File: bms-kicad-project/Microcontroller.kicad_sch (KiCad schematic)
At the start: 1 part, among them U2 RP2040

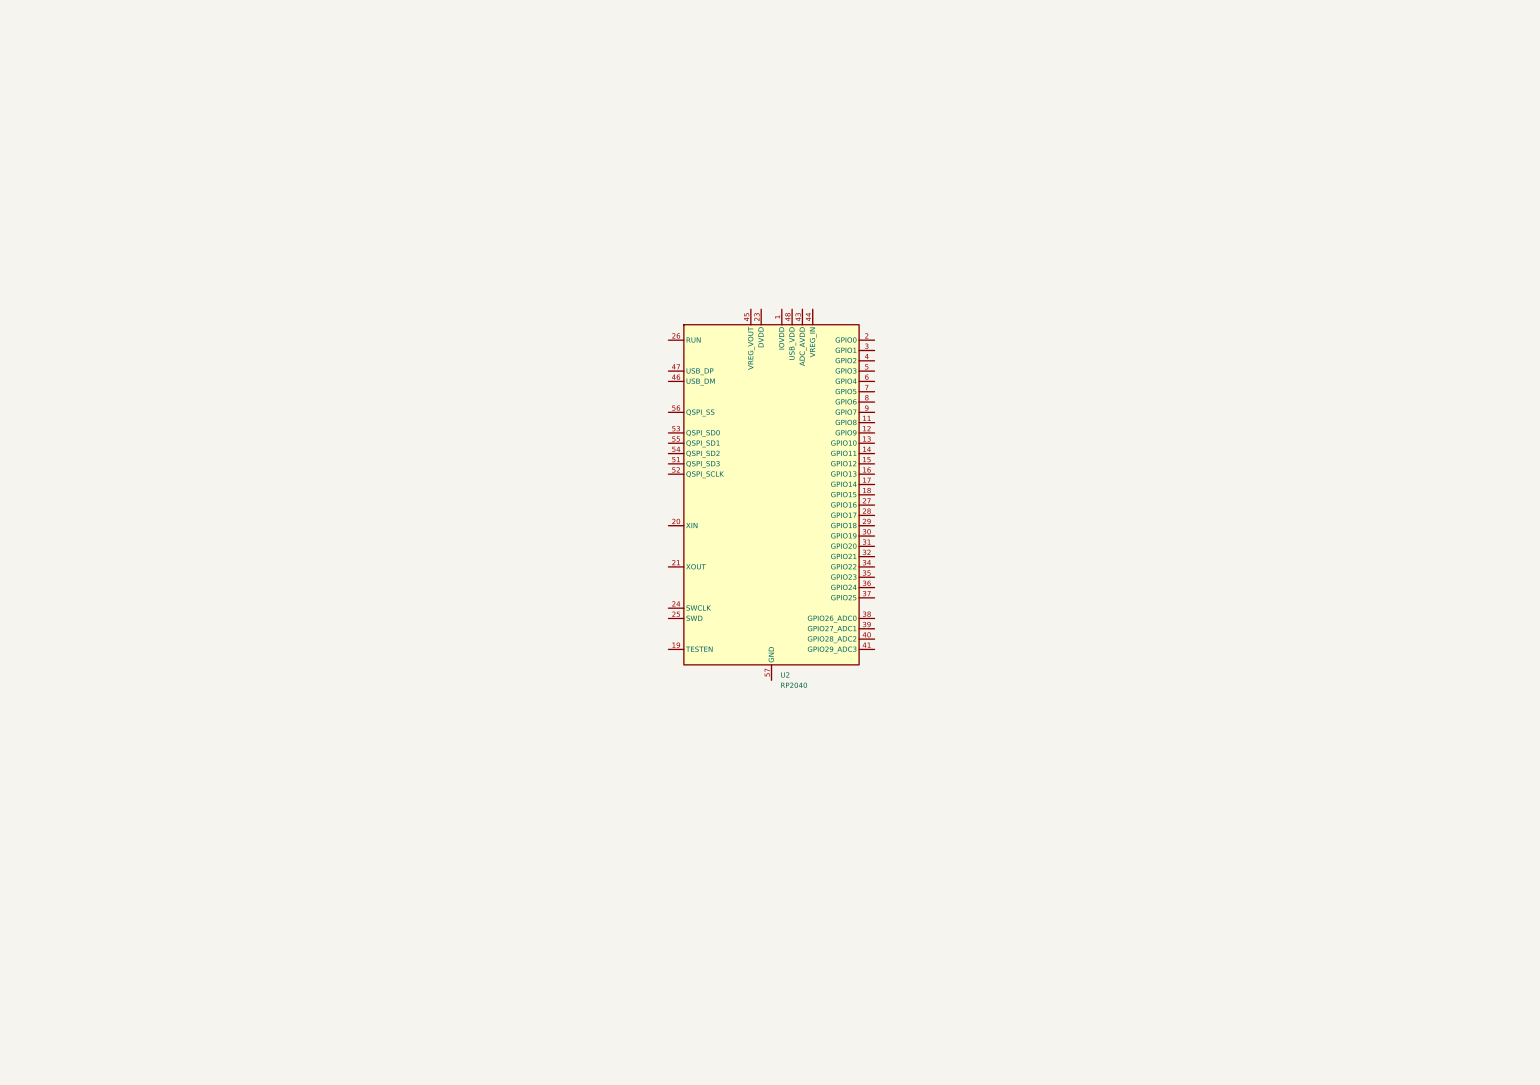
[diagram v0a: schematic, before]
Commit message: feat: added minimal MCU schematic, 3D component model folder
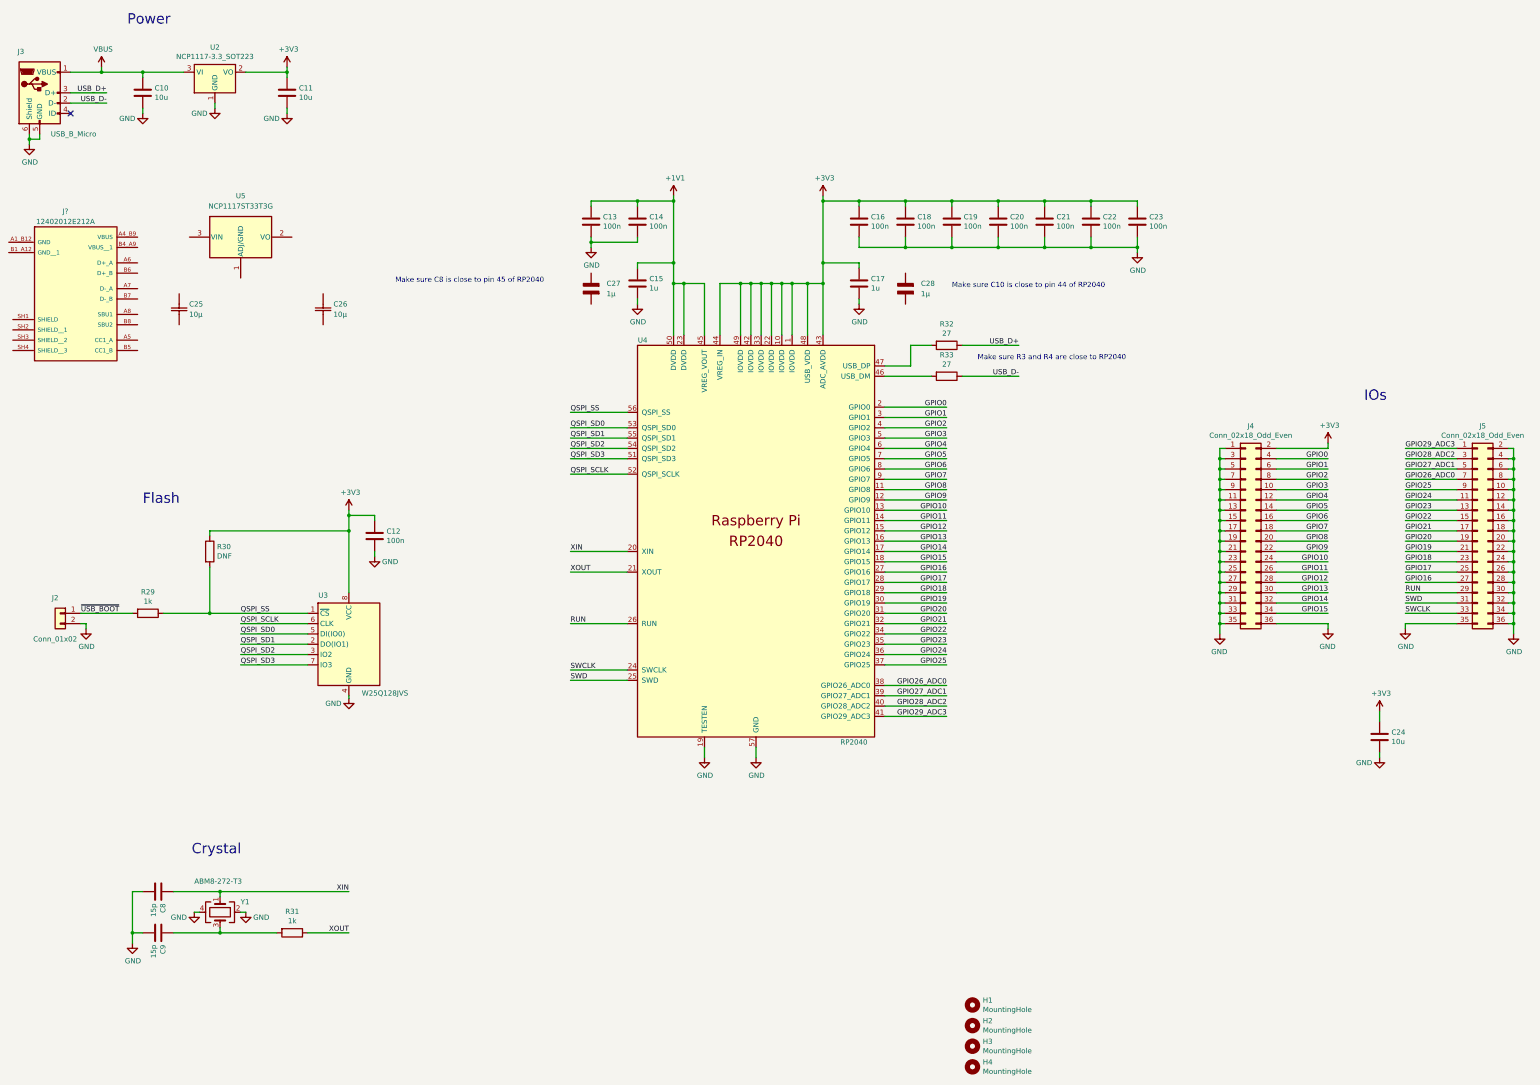
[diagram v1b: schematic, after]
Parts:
- removed U2: RP2040, Package_DFN_QFN:QFN-56-1EP_7x7mm_P0.4mm_EP3.2x3.2mm, symbol MCU_RaspberryPi:RP2040
- added C10, C11, C24: 10u, Capacitor_SMD:C_0805_2012Metric, symbol Device:C
- added C12, C13, C14, C16, C18, C19, C20, C21, C22, C23: 100n, Capacitor_SMD:C_0402_1005Metric, symbol Device:C
- added C15, C17: 1u, Capacitor_SMD:C_0402_1005Metric, symbol Device:C
- added C25, C26: 10µ, FixedWing:CAP_CL21B106KOQNNNE_SAM, symbol FixedWing:CL21B106KOQNNNE
- added C27, C28: 1µ, FixedWing:CAPC2012X140N, symbol FixedWing:GCM21BR71C105KA58L
- added C8, C9: 15p, Capacitor_SMD:C_0402_1005Metric, symbol Device:C
- added H1, H2, H3, H4: MountingHole, MountingHole:MountingHole_2.7mm_M2.5, symbol Mechanical:MountingHole
- added J2: Conn_01x02, Connector_PinHeader_2.54mm:PinHeader_1x02_P2.54mm_Vertical, symbol Connector_Generic:Conn_01x02
- added J3: USB_B_Micro, RP2040_minimal:USB_Micro-B_Amphenol_10103594-0001LF_Horizontal_modified, symbol Connector:USB_B_Micro
- added J4, J5: Conn_02x18_Odd_Even, Connector_PinHeader_2.54mm:PinHeader_2x18_P2.54mm_Vertical, symbol Connector_Generic:Conn_02x18_Odd_Even
- added J?: 12402012E212A, FixedWing:AMPHENOL_12402012E212A, symbol FixedWing:12402012E212A
- added R29, R31: 1k, Resistor_SMD:R_0402_1005Metric, symbol Device:R
- added R30: DNF, Resistor_SMD:R_0402_1005Metric, symbol Device:R
- added R32, R33: 27, Resistor_SMD:R_0402_1005Metric, symbol Device:R
- added U2: NCP1117-3.3_SOT223, Package_TO_SOT_SMD:SOT-223-3_TabPin2, symbol Regulator_Linear:NCP1117-3.3_SOT223
- added U3: W25Q128JVS, Package_SO:SOIC-8_5.23x5.23mm_P1.27mm, symbol Memory_Flash:W25Q128JVS
- added U4: RP2040, FixedWing:RP2040-QFN-56, symbol FixedWing:RP2040
- added U5: NCP1117ST33T3G, FixedWing:SOT223-3_ONS, symbol FixedWing:NCP1117ST33T3G
- added Y1: ABM8-272-T3, Crystal:Crystal_SMD_3225-4Pin_3.2x2.5mm, symbol Device:Crystal_GND24
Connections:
- new net: R33.2, U4.46 (USB_DM)
- new net: R32.2, U4.47 (USB_DP)
- new net: C9.1, R31.2, Y1.3
- new net +1V1: C13.1, C14.1, C15.1, U4.23 (DVDD), U4.45 (VREG_VOUT), U4.50 (DVDD)
- new net +3V3: C11.1, C12.1, C16.1, C17.1, C18.1, C19.1, C20.1, C21.1, C22.1, C23.1, C24.1, J4.2 (Pin_2), R30.1, U2.2 (VO), U3.8 (VCC), U4.1 (IOVDD), U4.10 (IOVDD), U4.22 (IOVDD), U4.33 (IOVDD), U4.42 (IOVDD), U4.43 (ADC_AVDD), U4.44 (VREG_IN), U4.48 (USB_VDD), U4.49 (IOVDD)
- new net GND: C10.2, C11.2, C12.2, C13.2, C14.2, C15.2, C16.2, C17.2, C18.2, C19.2, C20.2, C21.2, C22.2, C23.2, C24.2, C8.2, C9.2, J2.2 (Pin_2), J3.5 (GND), J3.6 (Shield), J4.1 (Pin_1), J4.11 (Pin_11), J4.13 (Pin_13), J4.15 (Pin_15), J4.17 (Pin_17), J4.19 (Pin_19), J4.21 (Pin_21), J4.23 (Pin_23), J4.25 (Pin_25), J4.27 (Pin_27), J4.29 (Pin_29), J4.3 (Pin_3), J4.31 (Pin_31), J4.33 (Pin_33), J4.35 (Pin_35), J4.36 (Pin_36), J4.5 (Pin_5), J4.7 (Pin_7), J4.9 (Pin_9), J5.10 (Pin_10), J5.12 (Pin_12), J5.14 (Pin_14), J5.16 (Pin_16), J5.18 (Pin_18), J5.2 (Pin_2), J5.20 (Pin_20), J5.22 (Pin_22), J5.24 (Pin_24), J5.26 (Pin_26), J5.28 (Pin_28), J5.30 (Pin_30), J5.32 (Pin_32), J5.34 (Pin_34), J5.35 (Pin_35), J5.36 (Pin_36), J5.4 (Pin_4), J5.6 (Pin_6), J5.8 (Pin_8), U2.1 (GND), U3.4 (GND), U4.19 (TESTEN), U4.57 (GND), Y1.2, Y1.4
- new net GPIO0: J4.4 (Pin_4), U4.2 (GPIO0)
- new net GPIO1: J4.6 (Pin_6), U4.3 (GPIO1)
- new net GPIO10: J4.24 (Pin_24), U4.13 (GPIO10)
- new net GPIO11: J4.26 (Pin_26), U4.14 (GPIO11)
- new net GPIO12: J4.28 (Pin_28), U4.15 (GPIO12)
- new net GPIO13: J4.30 (Pin_30), U4.16 (GPIO13)
- new net GPIO14: J4.32 (Pin_32), U4.17 (GPIO14)
- new net GPIO15: J4.34 (Pin_34), U4.18 (GPIO15)
- new net GPIO16: J5.27 (Pin_27), U4.27 (GPIO16)
- new net GPIO17: J5.25 (Pin_25), U4.28 (GPIO17)
- new net GPIO18: J5.23 (Pin_23), U4.29 (GPIO18)
- new net GPIO19: J5.21 (Pin_21), U4.30 (GPIO19)
- new net GPIO2: J4.8 (Pin_8), U4.4 (GPIO2)
- new net GPIO20: J5.19 (Pin_19), U4.31 (GPIO20)
- new net GPIO21: J5.17 (Pin_17), U4.32 (GPIO21)
- new net GPIO22: J5.15 (Pin_15), U4.34 (GPIO22)
- new net GPIO23: J5.13 (Pin_13), U4.35 (GPIO23)
- new net GPIO24: J5.11 (Pin_11), U4.36 (GPIO24)
- new net GPIO25: J5.9 (Pin_9), U4.37 (GPIO25)
- new net GPIO26_ADC0: J5.7 (Pin_7), U4.38 (GPIO26_ADC0)
- new net GPIO27_ADC1: J5.5 (Pin_5), U4.39 (GPIO27_ADC1)
- new net GPIO28_ADC2: J5.3 (Pin_3), U4.40 (GPIO28_ADC2)
- new net GPIO29_ADC3: J5.1 (Pin_1), U4.41 (GPIO29_ADC3)
- new net GPIO3: J4.10 (Pin_10), U4.5 (GPIO3)
- new net GPIO4: J4.12 (Pin_12), U4.6 (GPIO4)
- new net GPIO5: J4.14 (Pin_14), U4.7 (GPIO5)
- new net GPIO6: J4.16 (Pin_16), U4.8 (GPIO6)
- new net GPIO7: J4.18 (Pin_18), U4.9 (GPIO7)
- new net GPIO8: J4.20 (Pin_20), U4.11 (GPIO8)
- new net GPIO9: J4.22 (Pin_22), U4.12 (GPIO9)
- new net QSPI_SCLK: U3.6 (CLK), U4.52 (QSPI_SCLK)
- new net QSPI_SD0: U3.5 (DI(IO0)), U4.53 (QSPI_SD0)
- new net QSPI_SD1: U3.2 (DO(IO1)), U4.55 (QSPI_SD1)
- new net QSPI_SD2: U3.3 (IO2), U4.54 (QSPI_SD2)
- new net QSPI_SD3: U3.7 (IO3), U4.51 (QSPI_SD3)
- new net QSPI_SS: R29.1, R30.2, U3.1 (~{CS}), U4.56 (QSPI_SS)
- new net RUN: J5.29 (Pin_29), U4.26 (RUN)
- new net SWCLK: J5.33 (Pin_33), U4.24 (SWCLK)
- new net SWD: J5.31 (Pin_31), U4.25 (SWD)
- new net USB_D+: J3.3 (D+), R32.1
- new net USB_D-: J3.2 (D-), R33.1
- new net VBUS: C10.1, J3.1 (VBUS), U2.3 (VI)
- new net XIN: C8.1, U4.20 (XIN), Y1.1
- new net XOUT: R31.1, U4.21 (XOUT)
- new net ~{USB_BOOT}: J2.1 (Pin_1), R29.2
- no-connect marks 0 -> 1
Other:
- note added: "Crystal"
- note added: "Flash"
- note added: "IOs"
- note added: "Make sure C10 is close to pin 44 of RP2040"
- note added: "Make sure C8 is close to pin 45 of RP2040"
- note added: "Make sure R3 and R4 are close to RP2040"
- note added: "Power"

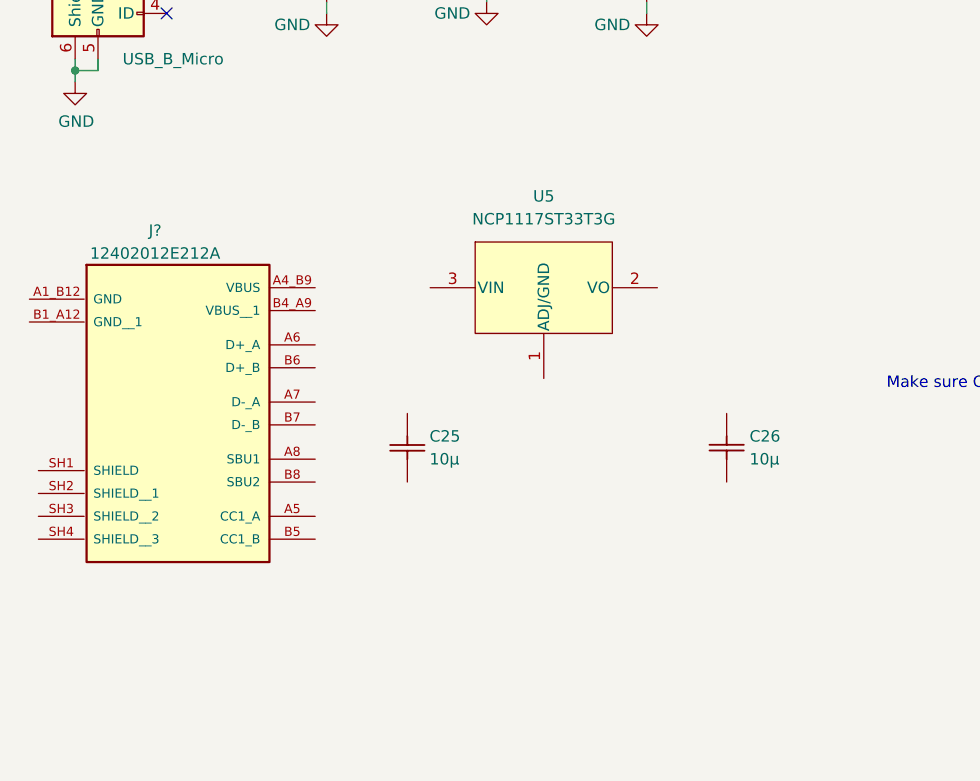
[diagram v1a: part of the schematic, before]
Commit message: feat: Added 3D models for connector and Flash ROM
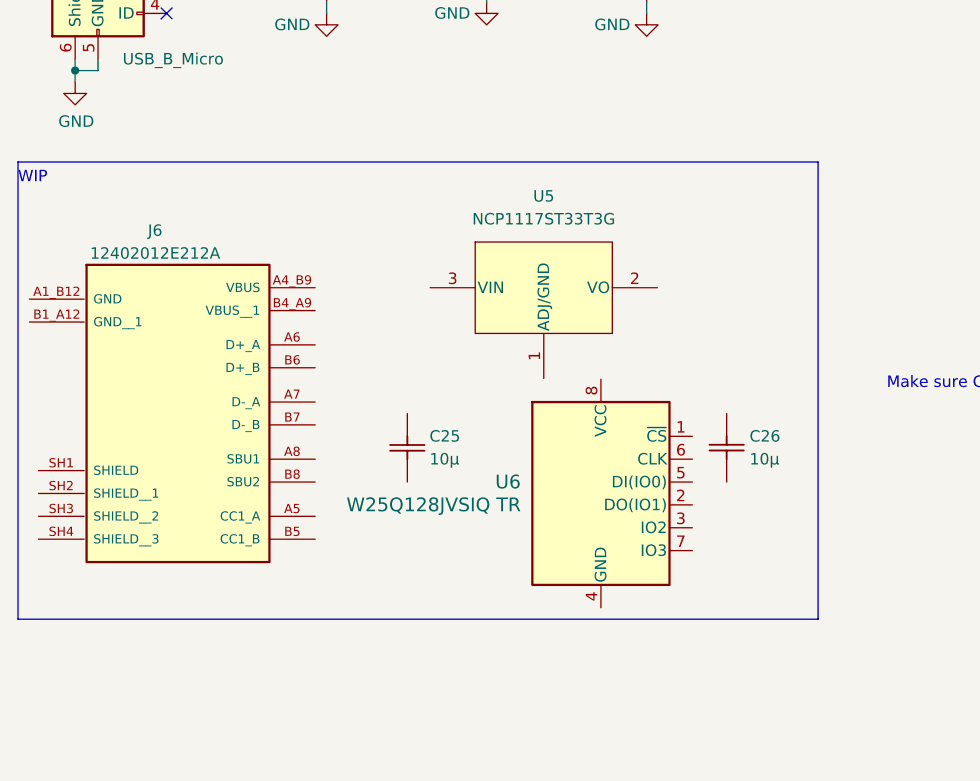
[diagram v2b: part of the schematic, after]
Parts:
- added U6: W25Q128JVSIQ TR, FixedWing:SOIC_208MIL_WIN, symbol FixedWing:W25Q128JVSIQ_TR
- gave numbers to parts that had none: 1
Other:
- note added: "WIP"
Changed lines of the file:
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@@
     (stroke (width 0) (type default))
+  )
+  (rectangle (start 99.06 55.88) (end 99.06 55.88)
+    (stroke (width 0) (type default))
+    (fill (type none))
+  )
+  (rectangle (start 12.7 55.88) (end 101.6 106.68)
+    (stroke (width 0) (type default))
+    (fill (type none))
   )
   (text "IOs" (at 347.98 110.49 0)
@@
   )
   (text "Make sure R3 and R4 are close to RP2040" (at 252.73 100.33 0)
+    (effects (font (size 1.27 1.27)) (justify left bottom))
+  )
+  (text "WIP" (at 12.7 58.42 0)
     (effects (font (size 1.27 1.27)) (justify left bottom))
   )
@@
   (symbol (lib_id "FixedWing:12402012E212A") (at 27.94 74.93 0) (unit 1)
     (in_bom yes) (on_board yes) (dnp no)
-    (property "Reference" "J?" (at 27.94 63.5 0)
+    (property "Reference" "J6" (at 27.94 63.5 0)
       (effects (font (size 1.27 1.27)))
     )
@@
       (project "bms-board"
         (path "/8a7831d1-a913-4f04-8780-225d2234b41d/449bb263-23d7-4f07-b4f7-6cd2e161d267"
-          (reference "J?") (unit 1)
+          (reference "J6") (unit 1)
         )
       )
@@
         )
       )
+    )
+  )
+  (symbol (lib_id "FixedWing:W25Q128JVSIQ_TR") (at 64.77 116.84 0) (unit 1)
+    (in_bom yes) (on_board yes) (dnp no) (fields_autoplaced)
+    (property "Reference" "U6" (at 68.58 91.44 0)
+      (effects (font (size 1.524 1.524)) (justify right))
+    )
+    (property "Value" "W25Q128JVSIQ TR" (at 68.58 93.98 0)
+      (effects (font (size 1.524 1.524)) (justify right))
+    )
+    (property "Footprint" "FixedWing:SOIC_208MIL_WIN" (at 52.07 96.52 0)
+      (effects (font (size 1.27 1.27) italic) hide)
+    )
+    (property "Datasheet" "https://www.winbond.com/resource-files/w25q128jv%20revf%2003272018%20plus.pdf" (at 52.07 93.98 0)
+      (effects (font (size 1.27 1.27) italic) hide)
+    )
+    (property "Manufacturer" "Winbond Electronics" (at 52.07 99.06 0)
+      (effects (font (size 1.27 1.27)) hide)
+    )
+    (property "Manufacturer_Part_Number" "W25Q128JVSIQ TR" (at 52.07 101.6 0)
+      (effects (font (size 1.27 1.27)) hide)
+    )
+    (pin "6")
+    (pin "8")
+    (pin "7")
+    (pin "5")
+    (pin "2")
+    (pin "3")
+    (pin "4")
+    (pin "1")
+    (instances
+      (project "bms-board"
+        (path "/8a7831d1-a913-4f04-8780-225d2234b41d/449bb263-23d7-4f07-b4f7-6cd2e161d267"
+          (reference "U6") (unit 1)
+        )
+      )
